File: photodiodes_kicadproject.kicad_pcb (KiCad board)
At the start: 4 copper layers, 55 x 30 mm, 39 parts, among them J1 Conn_01x03, Q1 Si2319CDS, U1 LM317_SOT-223, U2 LM337_SOT223, U3 TPS65131RGE

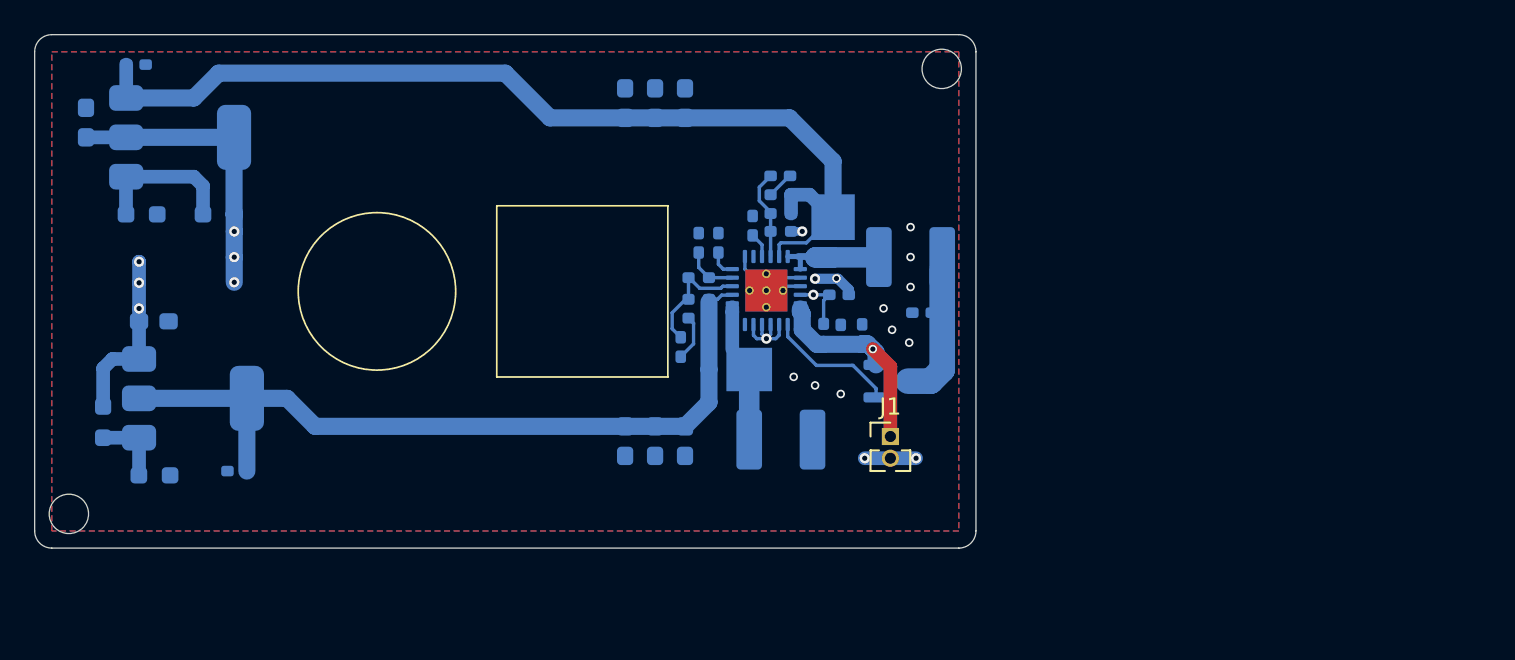
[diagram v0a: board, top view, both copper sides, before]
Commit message: Added photodiode circuit.
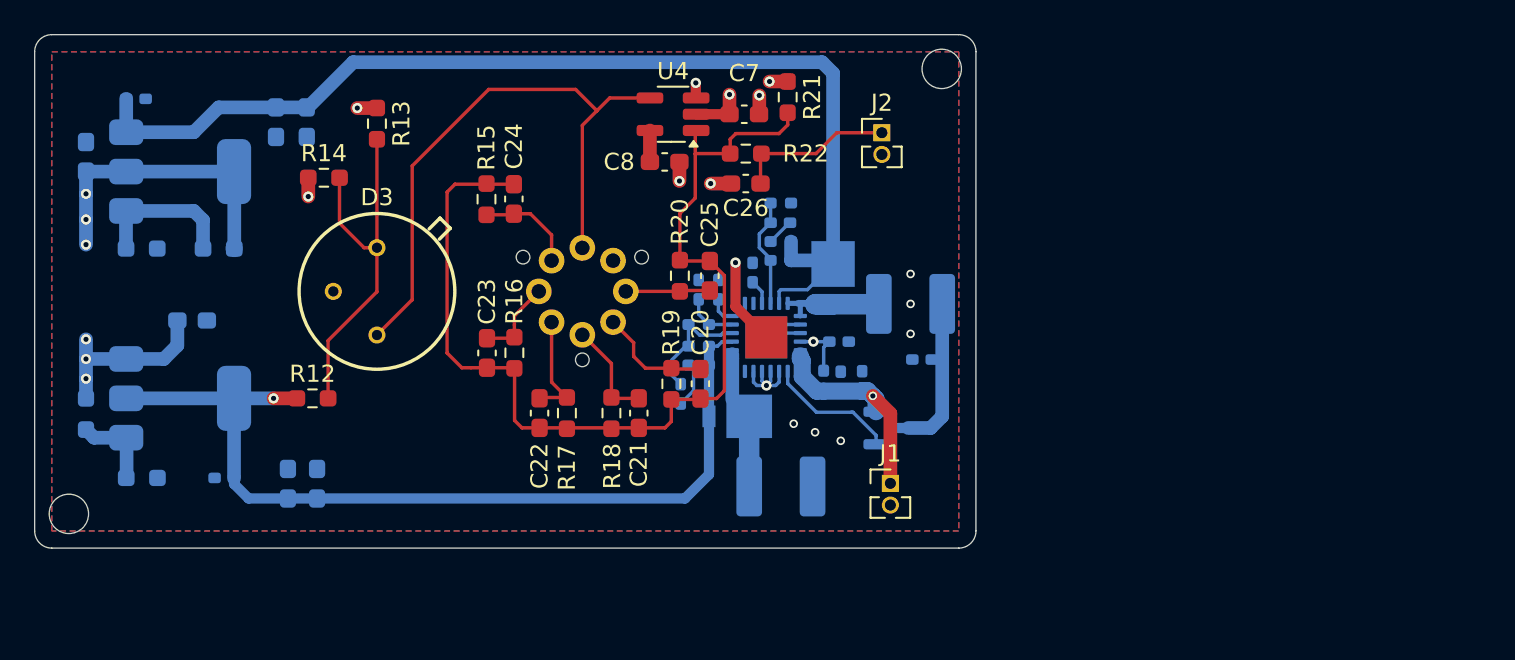
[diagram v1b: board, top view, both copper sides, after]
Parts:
- added C20: 10pF, Capacitor_SMD:C_0603_1608Metric_Pad1.08x0.95mm_HandSolder, F.Cu at (128.9, 105.4)
- added C21: 10pF, Capacitor_SMD:C_0603_1608Metric_Pad1.08x0.95mm_HandSolder, F.Cu at (125.3, 107.1)
- added C22: 10pF, Capacitor_SMD:C_0603_1608Metric_Pad1.08x0.95mm_HandSolder, F.Cu at (119.5, 107.1)
- added C23: 10pF, Capacitor_SMD:C_0603_1608Metric_Pad1.08x0.95mm_HandSolder, F.Cu at (116.4, 103.6)
- added C24: 10pF, Capacitor_SMD:C_0603_1608Metric_Pad1.08x0.95mm_HandSolder, F.Cu at (118.0, 94.6)
- added C25: 10pF, Capacitor_SMD:C_0603_1608Metric_Pad1.08x0.95mm_HandSolder, F.Cu at (129.4, 99.1)
- added C26: 100nF, Capacitor_SMD:C_0603_1608Metric_Pad1.08x0.95mm_HandSolder, F.Cu at (131.6, 93.7)
- added D3: FDS100, 1_MiscParts:FDS100, F.Cu at (110.0, 100.0)
- added J2: Conn_01x03, Connector_PinHeader_1.27mm:PinHeader_1x02_P1.27mm_Vertical, F.Cu at (139.5, 90.7)
- added R12: 0R, Resistor_SMD:R_0603_1608Metric_Pad0.98x0.95mm_HandSolder, F.Cu at (106.2, 106.2)
- added R13: 0R, Resistor_SMD:R_0603_1608Metric_Pad0.98x0.95mm_HandSolder, F.Cu at (110.0, 90.2)
- added R14: 0R, Resistor_SMD:R_0603_1608Metric_Pad0.98x0.95mm_HandSolder, F.Cu at (106.9, 93.4)
- added R15: 1K, Resistor_SMD:R_0603_1608Metric_Pad0.98x0.95mm_HandSolder, F.Cu at (116.4, 94.6)
- added R16: 3K, Resistor_SMD:R_0603_1608Metric_Pad0.98x0.95mm_HandSolder, F.Cu at (118.0, 103.6)
- added R17: 10K, Resistor_SMD:R_0603_1608Metric_Pad0.98x0.95mm_HandSolder, F.Cu at (121.1, 107.1)
- added R18: 30K, Resistor_SMD:R_0603_1608Metric_Pad0.98x0.95mm_HandSolder, F.Cu at (123.7, 107.1)
- added R19: 100K, Resistor_SMD:R_0603_1608Metric_Pad0.98x0.95mm_HandSolder, F.Cu at (127.2, 105.4)
- added R20: 150K, Resistor_SMD:R_0603_1608Metric_Pad0.98x0.95mm_HandSolder, F.Cu at (127.7, 99.1)
- added R21: 4K7, Resistor_SMD:R_0603_1608Metric_Pad0.98x0.95mm_HandSolder, F.Cu at (134.0, 88.7)
- added R22: 51R, Resistor_SMD:R_0603_1608Metric_Pad0.98x0.95mm_HandSolder, F.Cu at (131.6, 92.0)
- added SW1: SW_Rotary_1x6_MP, 1_Switches_TH:C&K_rm_submin_switch, B.Cu at (122.0, 100.0)
- added U4: OPA210, Package_TO_SOT_SMD:SOT-23-5_HandSoldering, F.Cu at (127.3, 89.7)
- C7, C8: moved to F.Cu
- moved C7 38.5 mm to (131.5, 89.7), turned to 0 degrees
- moved C18 35.1 mm to (93.0, 92.1)
- moved C8 31.3 mm to (126.8, 92.4), turned to 0 degrees
- moved C19 29.7 mm to (99.2, 101.7), turned to 180 degrees
- moved C14 20.4 mm to (104.1, 90.1), turned to -90 degrees
- moved C16 20.4 mm to (105.9, 90.1), turned to -90 degrees
- moved C17 19.9 mm to (106.5, 111.2), turned to 90 degrees
- moved C15 19.9 mm to (104.8, 111.2), turned to 90 degrees
- moved C10 2.74 mm to (128.8, 99.9)
- moved C11 2.74 mm to (129.9, 99.9)
- moved C9 2.74 mm to (131.9, 98.9)
- moved L2 2.74 mm to (133.6, 111.4)
- moved R10 2.74 mm to (133.6, 97.1)
- moved C12 2.74 mm to (127.8, 106.0)
- moved C13 2.74 mm to (133.6, 96.0)
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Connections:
- C1 pad 1: +9VDC -> +9V
- C14 pad 1: +9VDC -> +9V
- C15 pad 1: -9VDC -> -9V
- C16 pad 1: +9VDC -> +9V
- C17 pad 1: -9VDC -> -9V
- C18 pad 1: +9VDC -> +6V
- C19 pad 1: -9VDC -> GND
- C19 pad 2: GND -> -6V
- C2 pad 2: -9VDC -> -9V
- C7 pad 1: +6VDC -> -6V
- C8 pad 1: GND -> +6V
- C8 pad 2: -6VDC -> GND
- D1 pad 1: +9VDC -> +9V
- D2 pad 2: -9VDC -> -9V
- R10 pad 1: +9VDC -> +9V
- R11 pad 2: -9VDC -> -9V
- R4 pad 2: +6VDC -> +6V
- R5 pad 1: -6VDC -> -6V
- R7 pad 1: +9VDC -> +9V
- R9 pad 2: -9VDC -> -9V
- U1 pad 2: +6VDC -> +6V
- U1 pad 3: +9VDC -> +9V
- U2 pad 2: -9VDC -> -9V
- U2 pad 3: -6VDC -> -6V
- U3 pad 15: -9VDC -> -9V
- U3 pad 23: +9VDC -> +9V
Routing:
- net +9V: track 0.00 -> 64.5 mm
- net Net-(C20-Pad2): track 0.00 -> 59.9 mm
- net +9VDC: track 57.7 -> 0.00 mm
- net -9V: track 0.00 -> 52.6 mm, vias 0 -> 1
- net -9VDC: track 46.1 -> 0.00 mm
- net Net-(D3-K): track 0.00 -> 35.7 mm
- net Net-(D3-A): track 0.00 -> 21.8 mm
- net +6V: track 0.00 -> 19.3 mm, vias 0 -> 3
- net +6VDC: track 17.1 -> 0.00 mm, vias 3 -> 0
- net -6V: track 0.00 -> 14.1 mm, vias 0 -> 5
- net -6VDC: track 10.2 -> 0.00 mm, vias 3 -> 0
- net GND: track 8.72 -> 18.4 mm, vias 14 -> 13
- net Net-(J2-Pin_1): track 0.00 -> 9.31 mm
- net Net-(C20-Pad1): track 0.00 -> 6.71 mm
- net Net-(C22-Pad1): track 0.00 -> 6.40 mm
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- added copper zone on F.Cu, net +6V
- added copper zone on In2.Cu, net -6V
- removed copper zone on F.Cu, net +6VDC
- removed copper zone on In2.Cu, net -6VDC

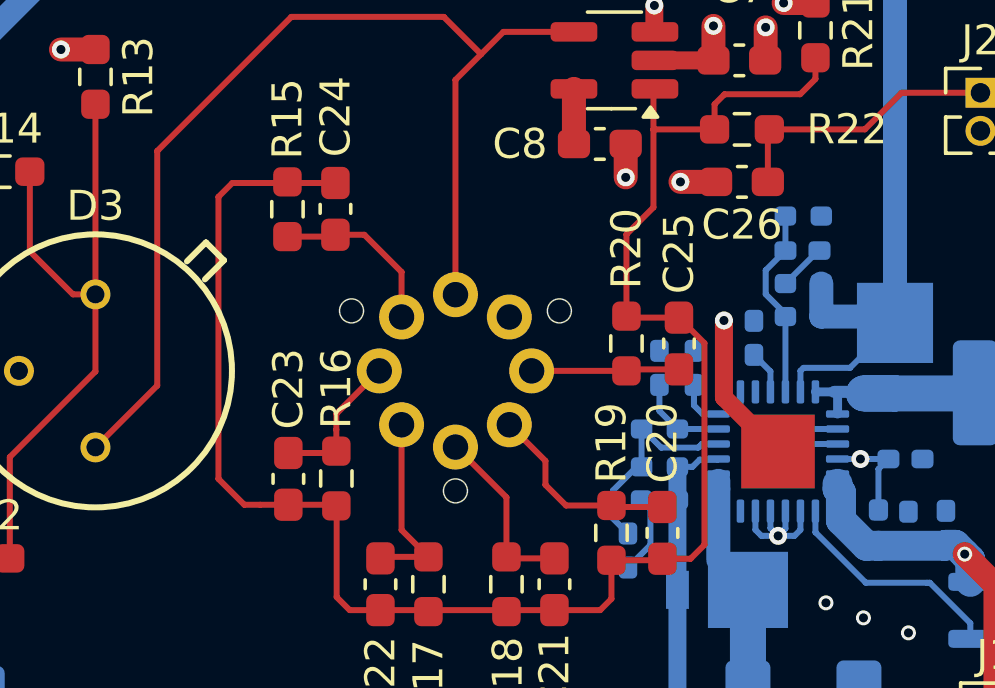
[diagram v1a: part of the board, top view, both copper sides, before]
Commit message: Added new branch. New branch for different +-9V power supply.
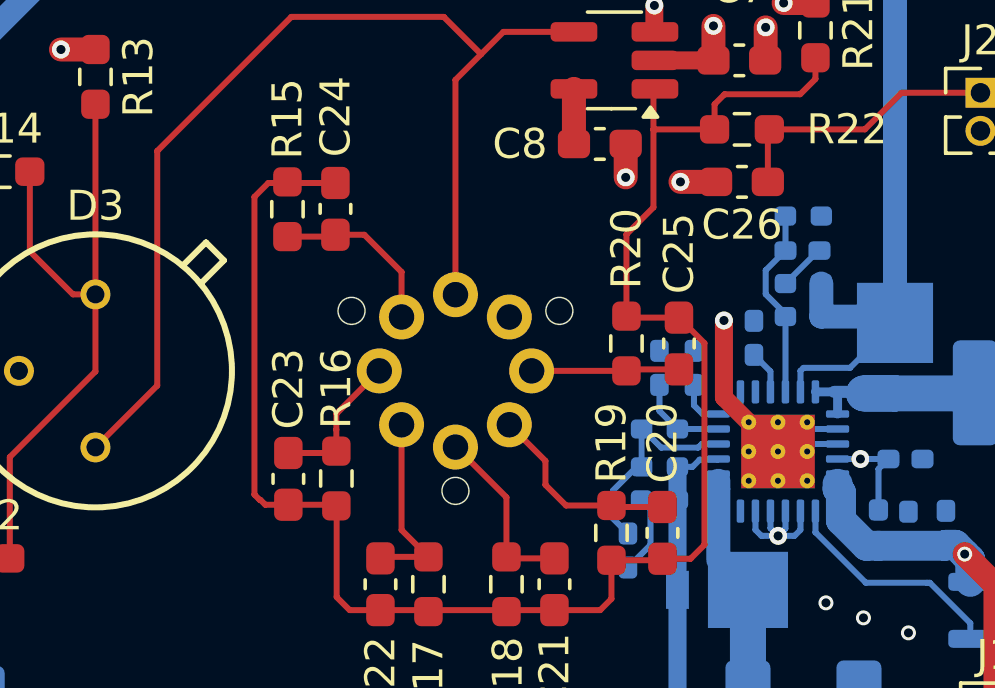
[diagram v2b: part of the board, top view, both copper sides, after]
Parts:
- D1, D2: footprint Diode_SMD:D_Powermite_AK -> Diode_SMD:D_Powermite_LargeCathode
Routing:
- net Net-(C20-Pad2): track 59.9 -> 57.8 mm

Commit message: Save progress.
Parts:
- removed C10: 220n, Capacitor_SMD:C_0402_1005Metric_Pad0.74x0.62mm_HandSolder
- removed C11: 4.7n, Capacitor_SMD:C_0402_1005Metric_Pad0.74x0.62mm_HandSolder
- removed C12, C13: 6.8p, Capacitor_SMD:C_0402_1005Metric_Pad0.74x0.62mm_HandSolder
- removed C4, C6: 100n, Capacitor_SMD:C_0402_1005Metric_Pad0.74x0.62mm_HandSolder
- removed C9: 10n, Capacitor_SMD:C_0402_1005Metric_Pad0.74x0.62mm_HandSolder
- removed Q1: Si2319CDS, Package_TO_SOT_SMD:SOT-23
- removed R10, R11: 51.1k, Resistor_SMD:R_0402_1005Metric_Pad0.72x0.64mm_HandSolder
- removed R3: 100R, Resistor_SMD:R_0402_1005Metric_Pad0.72x0.64mm_HandSolder
- removed R6: 162k, Resistor_SMD:R_0402_1005Metric_Pad0.72x0.64mm_HandSolder
- removed R7: 976k, Resistor_SMD:R_0402_1005Metric_Pad0.72x0.64mm_HandSolder
- removed R8: 150k, Resistor_SMD:R_0402_1005Metric_Pad0.72x0.64mm_HandSolder
- removed R9: 1.21M, Resistor_SMD:R_0402_1005Metric_Pad0.72x0.64mm_HandSolder
- removed U3: TPS65131RGE, Package_DFN_QFN:VQFN-24-1EP_4x4mm_P0.5mm_EP2.45x2.45mm_ThermalVias
- added U5: TES1-0519, Converter_DCDC:Converter_DCDC_TRACO_TES1-051x_121x_241x_Single_SMD, B.Cu at (135.7, 92.9)
- added U6: TES1-0519, Converter_DCDC:Converter_DCDC_TRACO_TES1-051x_121x_241x_Single_SMD, B.Cu at (135.6, 106.1)
- moved C3 31.4 mm to (169.1, 111.6)
- moved C5 31.4 mm to (172.6, 110.4)
- moved L2 31.4 mm to (164.3, 117.8)
- moved D1 31.4 mm to (167.4, 105.5)
- moved D2 31.4 mm to (161.8, 113.7)
- moved L1 31.4 mm to (171.9, 107.1)
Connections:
- C14 pad 2: GND -> GND2
- C15 pad 2: GND -> GND2
- C16 pad 2: GND -> GND2
- C17 pad 2: GND -> GND2
- C3 pad 1: /Power Input/+5VIN -> Net-(U5-+Vin)
- C5 pad 1: Net-(Q1-D) -> Net-(U6-+Vin)
- D1 pad 2: Net-(D1-A) -> GND2
- D2 pad 1: Net-(D2-K) -> GND2
- L1 pad 1: Net-(Q1-D) -> /Power Input/+5VIN
- L1 pad 2: Net-(D1-A) -> Net-(U5-+Vin)
- L2 pad 1: Net-(D2-K) -> /Power Input/+5VIN
- L2 pad 2: GND -> Net-(U6-+Vin)
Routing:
- net +9V: track 64.5 -> 16.9 mm
- net /Voltage Regulator/VIN: track 12.2 -> 0.00 mm, vias 2 -> 0
- net GND: track 18.4 -> 6.43 mm, vias 13 -> 6
- net -9V: track 52.6 -> 41.7 mm
- net Net-(D2-K): track 8.14 -> 0.00 mm
- net Net-(Q1-D): track 8.12 -> 0.00 mm
- net Net-(Q1-G): track 7.65 -> 0.00 mm
- net Net-(D1-A): track 7.46 -> 0.00 mm
- net Net-(U3-FBN): track 7.14 -> 0.00 mm
- net /Power Input/+5VIN: track 12.4 -> 5.53 mm, vias 1 -> 0
- net Net-(U3-FBP): track 6.59 -> 0.00 mm
- net Net-(U3-VREF): track 3.08 -> 0.00 mm
- net Net-(C12-Pad2): track 2.73 -> 0.00 mm
- net Net-(U3-CN): track 1.61 -> 0.00 mm
- net Net-(C13-Pad1): track 1.59 -> 0.00 mm
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
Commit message: Save progress.
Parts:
- removed C14, C15, C16, C17, C18, C19: 10u, Capacitor_SMD:C_0603_1608Metric_Pad1.08x0.95mm_HandSolder
- removed D1, D2: MBRM120ET1G, Diode_SMD:D_Powermite_LargeCathode
- removed L1, L2: 4.7u, 1_L_SMD:L_Bourns_SRP4021HMT
- removed R12: 0R, Resistor_SMD:R_0603_1608Metric_Pad0.98x0.95mm_HandSolder
- removed R18: 30K, Resistor_SMD:R_0603_1608Metric_Pad0.98x0.95mm_HandSolder
- removed U1: LM317_SOT-223, Package_TO_SOT_SMD:SOT-223-3_TabPin2
- removed U2: LM337_SOT223, Package_TO_SOT_SMD:SOT-223-3_TabPin2
- removed U5, U6: TES1-0519, Converter_DCDC:Converter_DCDC_TRACO_TES1-051x_121x_241x_Single_SMD
- added C4: 10nF, Capacitor_SMD:C_0402_1005Metric_Pad0.74x0.62mm_HandSolder, F.Cu at (100.4, 96.9)
- added R3: 40K2, Resistor_SMD:R_0402_1005Metric_Pad0.72x0.64mm_HandSolder, F.Cu at (98.4, 96.4)
- added U3: LTC3260xDE, Package_DFN_QFN:DFN-14-1EP_3x4mm_P0.5mm_EP1.7x3.3mm, F.Cu at (99.0, 100.0)
- C1: value 100n -> 1uF; moved to F.Cu
- C2: value 100n -> 10uF; footprint Capacitor_SMD:C_0402_1005Metric_Pad0.74x0.62mm_HandSolder -> Capacitor_SMD:C_0603_1608Metric_Pad1.08x0.95mm_HandSolder; moved to F.Cu
- C20, C21, C22, C23, C24, C25: value 10pF -> 5.6pF; footprint Capacitor_SMD:C_0603_1608Metric_Pad1.08x0.95mm_HandSolder -> Capacitor_SMD:C_0402_1005Metric_Pad0.74x0.62mm_HandSolder
- C3: value 4.7u -> 10uF; footprint Capacitor_SMD:C_0402_1005Metric_Pad0.74x0.62mm_HandSolder -> Capacitor_SMD:C_0603_1608Metric_Pad1.08x0.95mm_HandSolder; moved to F.Cu
- C5: value 4.7u -> 10nF; moved to F.Cu
- J2: value Conn_01x03 -> Conn_BNC; footprint Connector_PinHeader_1.27mm:PinHeader_1x02_P1.27mm_Vertical -> 1_Conn_RF:BNC_panel_mount
- R1: value 680R -> 40K2; footprint Resistor_SMD:R_0603_1608Metric_Pad0.98x0.95mm_HandSolder -> Resistor_SMD:R_0402_1005Metric_Pad0.72x0.64mm_HandSolder; moved to F.Cu
- R15, R16, R17, R19, R20: footprint Resistor_SMD:R_0603_1608Metric_Pad0.98x0.95mm_HandSolder -> Resistor_SMD:R_0402_1005Metric_Pad0.72x0.64mm_HandSolder
- R2: value 680R -> 10K; footprint Resistor_SMD:R_0603_1608Metric_Pad0.98x0.95mm_HandSolder -> Resistor_SMD:R_0402_1005Metric_Pad0.72x0.64mm_HandSolder; moved to F.Cu
- R4: value 180R -> 10K; footprint Resistor_SMD:R_0603_1608Metric_Pad0.98x0.95mm_HandSolder -> Resistor_SMD:R_0402_1005Metric_Pad0.72x0.64mm_HandSolder; moved to F.Cu
- R5: value 180R -> 30K; footprint Resistor_SMD:R_0603_1608Metric_Pad0.98x0.95mm_HandSolder -> Resistor_SMD:R_0402_1005Metric_Pad0.72x0.64mm_HandSolder; moved to F.Cu
- moved C3 74.4 mm to (96.3, 96.2)
- moved C5 70.6 mm to (102.5, 101.5), turned to 0 degrees
- moved R5 30.7 mm to (123.7, 107.1), turned to 90 degrees
- moved C1 11.3 mm to (96.2, 100.0), turned to 90 degrees
- moved R2 9.29 mm to (101.6, 103.3), turned to 90 degrees
- moved C2 8.06 mm to (95.9, 104.7)
- moved R1 6.91 mm to (99.1, 103.8)
- moved J1 4.00 mm to (137.2, 108.4)
- moved C8 2.98 mm to (124.0, 91.5), turned to -90 degrees
- moved J2 2.28 mm to (139.7, 93.0)
- moved R16 1.83 mm to (116.2, 103.6)
- moved R4 1.70 mm to (100.4, 95.8)
- moved C22 1.50 mm to (121.0, 107.1)
- moved R17 1.20 mm to (119.9, 107.1)
- moved C23 0.87 mm to (117.3, 103.6)
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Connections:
- C1 pad 1: +9V -> Net-(U3-C^{+})
- C1 pad 2: GND -> Net-(U3-C^{-})
- C2 pad 2: -9V -> /Power Input/+12VIN
- J1 pad 1: /Power Input/+5VIN -> /Power Input/+12VIN
- R1 pad 1: GND -> Net-(U3-ADJ^{+})
- R1 pad 2: Net-(U1-ADJ) -> +6V
- R2 pad 1: Net-(U2-ADJ) -> GND
- R2 pad 2: GND -> Net-(U3-ADJ^{+})
- R4 pad 1: Net-(U1-ADJ) -> Net-(U3-ADJ^{-})
- R4 pad 2: +6V -> GND
- R5 pad 1: -6V -> Net-(C20-Pad2)
- R5 pad 2: Net-(U2-ADJ) -> Net-(C21-Pad1)
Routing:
- net /Power Input/+12VIN: track 0.00 -> 65.0 mm, vias 0 -> 3
- net -9V: track 41.7 -> 0.00 mm, vias 1 -> 0
- net -6V: track 14.1 -> 46.0 mm, vias 5 -> 0
- net +6V: track 19.3 -> 40.3 mm, vias 3 -> 0
- net GND: track 6.43 -> 27.1 mm, vias 6 -> 19
- net +9V: track 16.9 -> 0.00 mm
- net Net-(D3-A): track 21.8 -> 11.8 mm
- net Net-(U1-ADJ): track 8.58 -> 0.00 mm
- net /Power Input/+5VIN: track 5.53 -> 0.00 mm
- net Net-(U2-ADJ): track 4.90 -> 0.00 mm
- net Net-(U3-ADJ^{-}): track 0.00 -> 4.18 mm
- net Net-(U3-ADJ^{+}): track 0.00 -> 3.99 mm
- net Net-(U3-V_{OUT}): track 0.00 -> 2.59 mm
- net Net-(U3-C^{-}): track 0.00 -> 2.06 mm
- net Net-(U3-C^{+}): track 0.00 -> 1.90 mm
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- removed copper zone on F.Cu, net +6V
- removed copper zone on In2.Cu, net -6V
- removed copper zone on In1.Cu, net GND
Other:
- copper layers 4 -> 2
- board text added: "FDS100"
- board text added: "Photodiode: design2"
- board text added: "Power In +12V"

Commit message: Added fabrication files. Board finalized.
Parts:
- added G***: LOGO, LOGO, F.Cu at (115.1, 110.8)
- added G***: LOGO, LOGO, B.Cu at (116.3, 109.9)
- added G***: LOGO, LOGO, B.Cu at (98.7, 100.0)
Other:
- board text added: "C"
- board text added: "H"

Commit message: Updated pcb. Added render image. Added pcb step file.
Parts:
- moved J2 0.50 mm to (139.7, 93.5)
